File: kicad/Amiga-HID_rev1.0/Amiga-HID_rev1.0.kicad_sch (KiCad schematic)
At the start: 59 parts, among them J1 USB-A Host, J2 JST-XH-5A, J3 OLED I2C, J4 Reserve 3V3+GP+GND+VSYS, J5 JST-SH-3 SWD, J6 JST-SH-3 UART, J7 Conn_01x06_Pin, SW1 Boot, SW2 Run, U1 USBLC6-2SC6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

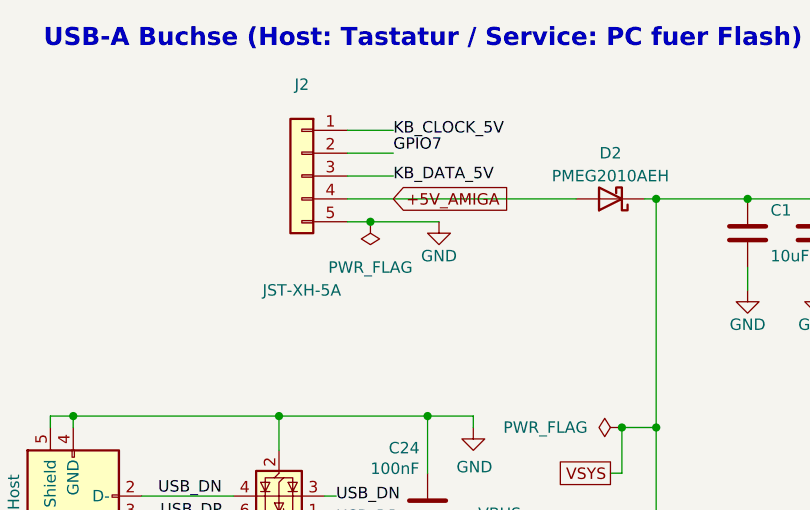
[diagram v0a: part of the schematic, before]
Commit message: J6 war spiegelverkehrt
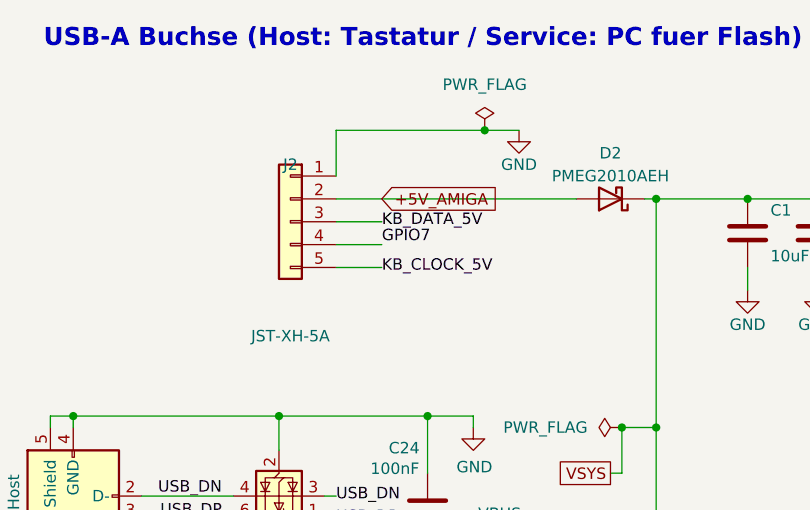
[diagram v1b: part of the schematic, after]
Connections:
- net +5V_AMIGA: now also J2.2 (Pin_2); no longer J2.4 (Pin_4)
- net GND: now also J2.1 (Pin_1); no longer J2.5 (Pin_5)
- net GPIO7: now also J2.4 (Pin_4); no longer J2.2 (Pin_2)
- net KB_CLOCK_5V: now also J2.5 (Pin_5); no longer J2.1 (Pin_1)
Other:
- moved on the sheet: J2
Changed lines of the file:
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@@
 	)
 	(junction
-		(at 54.61 40.64)
-		(diameter 0)
-		(color 0 0 0 0)
-	)
-	(junction
 		(at 86.36 78.74)
 		(diameter 0)
@@
 	)
 	(junction
+		(at 67.31 30.48)
+		(diameter 0)
+		(color 0 0 0 0)
+	)
+	(junction
 		(at 217.17 85.09)
 		(diameter 0)
@@
 	(wire
 		(pts
+			(xy 50.8 30.48) (xy 67.31 30.48)
+		)
+		(stroke
+			(width 0)
+			(type default)
+		)
+	)
+	(wire
+		(pts
 			(xy 195.58 256.54) (xy 201.93 256.54)
 		)
@@
 	(wire
 		(pts
-			(xy 52.07 30.48) (xy 57.15 30.48)
-		)
-		(stroke
-			(width 0)
-			(type default)
-		)
-	)
-	(wire
-		(pts
 			(xy 201.93 250.19) (xy 215.9 250.19)
 		)
@@
 	(wire
 		(pts
+			(xy 50.8 45.72) (xy 55.88 45.72)
+		)
+		(stroke
+			(width 0)
+			(type default)
+		)
+	)
+	(wire
+		(pts
 			(xy 195.58 64.77) (xy 195.58 85.09)
 		)
@@
 	(wire
 		(pts
-			(xy 52.07 35.56) (xy 57.15 35.56)
-		)
-		(stroke
-			(width 0)
-			(type default)
-		)
-	)
-	(wire
-		(pts
 			(xy 151.13 246.38) (xy 158.75 246.38)
 		)
@@
 	(wire
 		(pts
+			(xy 50.8 43.18) (xy 55.88 43.18)
+		)
+		(stroke
+			(width 0)
+			(type default)
+		)
+	)
+	(wire
+		(pts
 			(xy 85.09 154.94) (xy 101.6 154.94)
 		)
@@
 	(wire
 		(pts
+			(xy 50.8 30.48) (xy 50.8 35.56)
+		)
+		(stroke
+			(width 0)
+			(type default)
+		)
+	)
+	(wire
+		(pts
 			(xy 166.37 93.98) (xy 173.99 93.98)
 		)
@@
 	(wire
 		(pts
+			(xy 50.8 40.64) (xy 55.88 40.64)
+		)
+		(stroke
+			(width 0)
+			(type default)
+		)
+	)
+	(wire
+		(pts
 			(xy 186.69 182.88) (xy 172.72 182.88)
 		)
@@
 	(wire
 		(pts
-			(xy 54.61 40.64) (xy 62.23 40.64)
+			(xy 67.31 30.48) (xy 71.12 30.48)
 		)
 		(stroke
@@
 	(wire
 		(pts
-			(xy 52.07 38.1) (xy 77.47 38.1)
-		)
-		(stroke
-			(width 0)
-			(type default)
-		)
-	)
-	(wire
-		(pts
 			(xy 195.58 63.5) (xy 195.58 64.77)
 		)
@@
 	(wire
 		(pts
+			(xy 50.8 38.1) (xy 77.47 38.1)
+		)
+		(stroke
+			(width 0)
+			(type default)
+		)
+	)
+	(wire
+		(pts
 			(xy 266.7 76.2) (xy 255.27 76.2)
 		)
@@
 	(wire
 		(pts
-			(xy 52.07 33.02) (xy 57.15 33.02)
-		)
-		(stroke
-			(width 0)
-			(type default)
-		)
-	)
-	(wire
-		(pts
 			(xy 52.07 186.69) (xy 83.82 186.69)
 		)
@@
 	(wire
 		(pts
-			(xy 52.07 40.64) (xy 54.61 40.64)
-		)
-		(stroke
-			(width 0)
-			(type default)
-		)
-	)
-	(wire
-		(pts
 			(xy 162.56 106.68) (xy 154.94 106.68)
 		)
@@
 	)
 	(label "KB_CLOCK_5V"
-		(at 57.15 30.48 0)
+		(at 55.88 45.72 0)
 		(effects
 			(font
@@
 	)
 	(label "GPIO7"
-		(at 57.15 33.02 0)
+		(at 55.88 43.18 0)
 		(effects
 			(font
@@
 	)
 	(label "KB_DATA_5V"
-		(at 57.15 35.56 0)
+		(at 55.88 40.64 0)
 		(effects
 			(font
@@
 	(global_label "+5V_AMIGA"
 		(shape input)
-		(at 57.15 38.1 0)
+		(at 55.88 38.1 0)
 		(fields_autoplaced yes)
 		(effects
@@
 		)
 		(property "Intersheetrefs" "${INTERSHEET_REFS}"
-			(at 57.15 38.1 0)
+			(at 55.88 38.1 0)
 			(hide yes)
 			(show_name no)
@@
 	(symbol
 		(lib_id "Connector_Generic:Conn_01x05")
-		(at 46.99 35.56 0)
+		(at 45.72 40.64 0)
 		(mirror y)
 		(unit 1)
@@
 		(dnp no)
 		(property "Reference" "J2"
-			(at 46.99 25.4 0)
+			(at 45.72 34.29 0)
 			(show_name no)
 			(do_not_autoplace no)
@@
 		)
 		(property "Value" "JST-XH-5A"
-			(at 46.99 48.26 0)
+			(at 45.72 53.34 0)
 			(show_name no)
 			(do_not_autoplace no)
@@
 		)
 		(property "Footprint" "Connector_JST:JST_XH_B5B-XH-A_1x05_P2.50mm_Vertical"
-			(at 46.99 35.56 0)
+			(at 45.72 40.64 0)
 			(hide yes)
 			(show_name no)
@@
 		)
 		(property "Datasheet" ""
-			(at 46.99 35.56 0)
+			(at 45.72 40.64 0)
 			(hide yes)
 			(show_name no)
@@
 		)
 		(property "Description" "Generic connector, single row, 01x05, script generated (kicad-library-utils/schlib/autogen/connector/)"
-			(at 46.99 35.56 0)
+			(at 45.72 40.64 0)
 			(hide yes)
 			(show_name no)
@@
 		)
 		(property "LCSC" "C157932"
-			(at 46.99 35.56 0)
+			(at 45.72 40.64 0)
 			(hide yes)
 			(show_name no)
@@
 	(symbol
 		(lib_id "power:GND")
-		(at 62.23 40.64 0)
+		(at 71.12 30.48 0)
 		(unit 1)
 		(body_style 1)
@@
 		(fields_autoplaced yes)
 		(property "Reference" "#PWR02"
-			(at 62.23 46.99 0)
+			(at 71.12 36.83 0)
 			(hide yes)
 			(show_name no)
@@
 		)
 		(property "Value" "GND"
-			(at 62.23 44.45 0)
+			(at 71.12 34.29 0)
 			(show_name no)
 			(do_not_autoplace no)
@@
 		)
 		(property "Footprint" ""
-			(at 62.23 40.64 0)
+			(at 71.12 30.48 0)
 			(hide yes)
 			(show_name no)
@@
 		)
 		(property "Datasheet" ""
-			(at 62.23 40.64 0)
+			(at 71.12 30.48 0)
 			(hide yes)
 			(show_name no)
@@
 		)
 		(property "Description" "Power symbol creates a global label with name \"GND\" , ground"
-			(at 62.23 40.64 0)
+			(at 71.12 30.48 0)
 			(hide yes)
 			(show_name no)
@@
 	(symbol
 		(lib_id "power:PWR_FLAG")
-		(at 54.61 40.64 0)
-		(mirror x)
+		(at 67.31 30.48 0)
 		(unit 1)
 		(body_style 1)
@@
 		(dnp no)
 		(property "Reference" "#FLG01"
-			(at 54.61 42.545 0)
+			(at 67.31 28.575 0)
 			(hide yes)
 			(show_name no)
@@
 		)
 		(property "Value" "PWR_FLAG"
-			(at 54.61 45.72 0)
+			(at 67.31 25.4 0)
 			(show_name no)
 			(do_not_autoplace no)
@@
 		)
 		(property "Footprint" ""
-			(at 54.61 40.64 0)
+			(at 67.31 30.48 0)
 			(hide yes)
 			(show_name no)
@@
 		)
 		(property "Datasheet" ""
-			(at 54.61 40.64 0)
+			(at 67.31 30.48 0)
 			(hide yes)
 			(show_name no)
@@
 		)
 		(property "Description" "Special symbol for telling ERC where power comes from"
-			(at 54.61 40.64 0)
+			(at 67.31 30.48 0)
 			(hide yes)
 			(show_name no)
